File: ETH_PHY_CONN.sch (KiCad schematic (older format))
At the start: 63 parts, among them J2 RJMG2012211A0FR, U7 DP83869HMRGZT, Y1 XRCGE25M000FBA1AR0

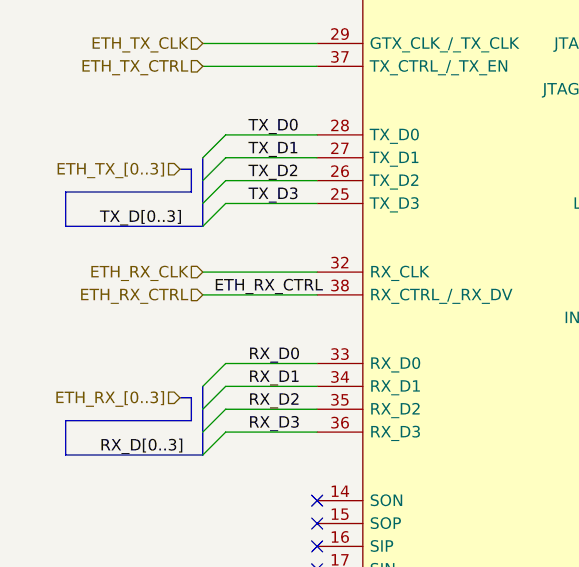
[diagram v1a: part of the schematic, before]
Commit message: Connected USB2 connections with FPGA and updated the top sheet
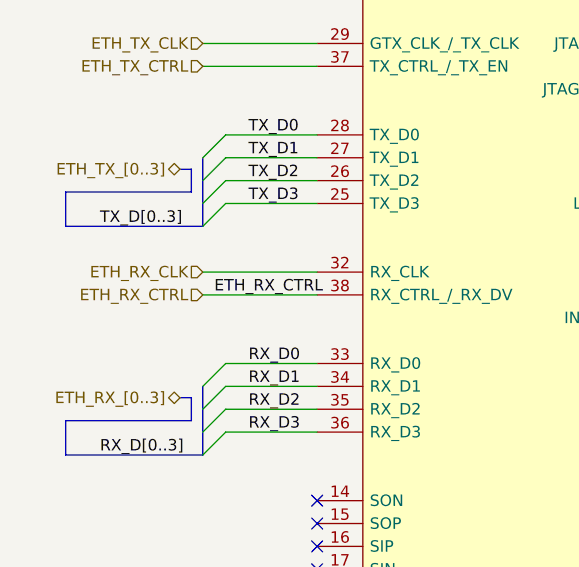
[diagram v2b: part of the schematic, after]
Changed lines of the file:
@@
 $Descr A4 11693 8268
 encoding utf-8
-Sheet 10 22
+Sheet 9 22
 Title ""
 Date ""
@@
 Entry Wire Line
 	1200 5400 1300 5300
-Text HLabel 1100 5450 0    50   Input ~ 0
+Text HLabel 1100 5450 0    50   BiDi ~ 0
 ETH_TX_[0..3]
 Text Label 750  5700 0    50   ~ 0
@@
 Entry Wire Line
 	1200 6400 1300 6300
-Text HLabel 1100 6450 0    50   Input ~ 0
+Text HLabel 1100 6450 0    50   BiDi ~ 0
 ETH_RX_[0..3]
 Text Label 750  6700 0    50   ~ 0

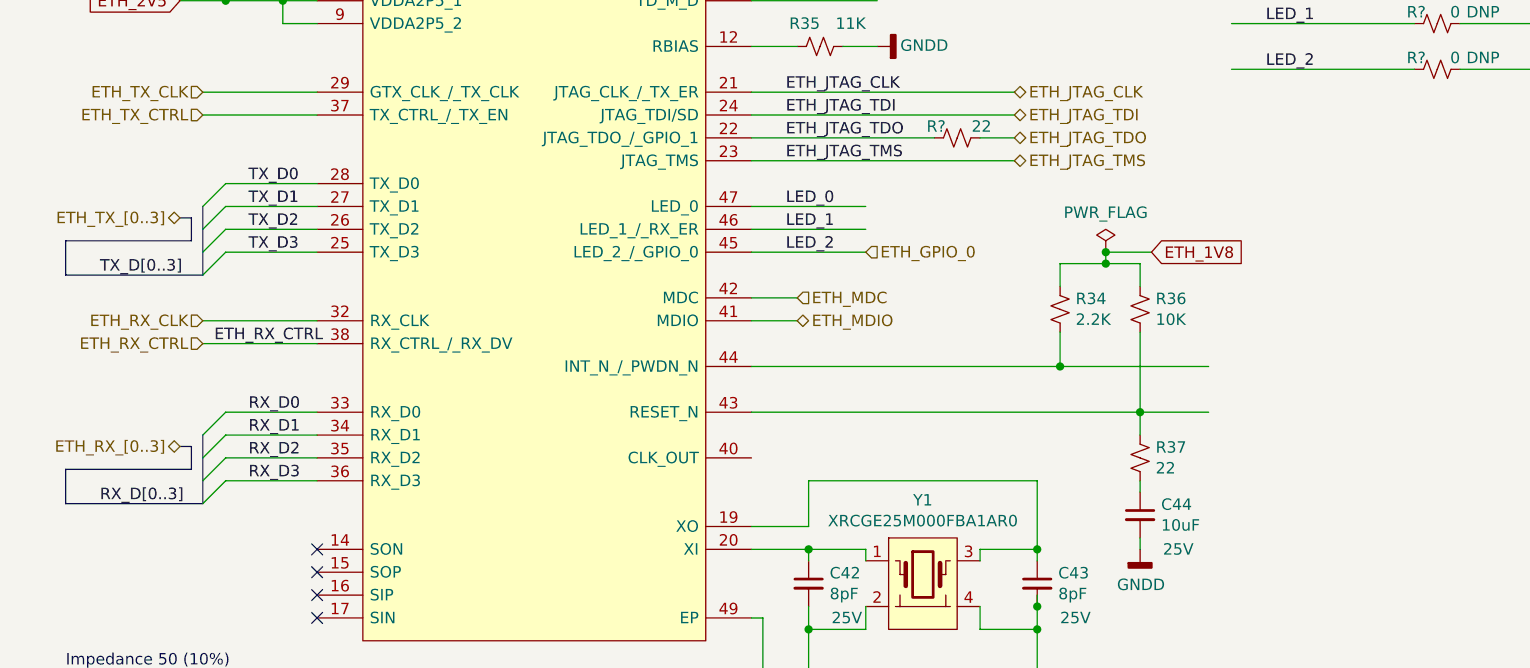
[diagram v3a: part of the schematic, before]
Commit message: Connected Ethernet sheet with FPGA bank
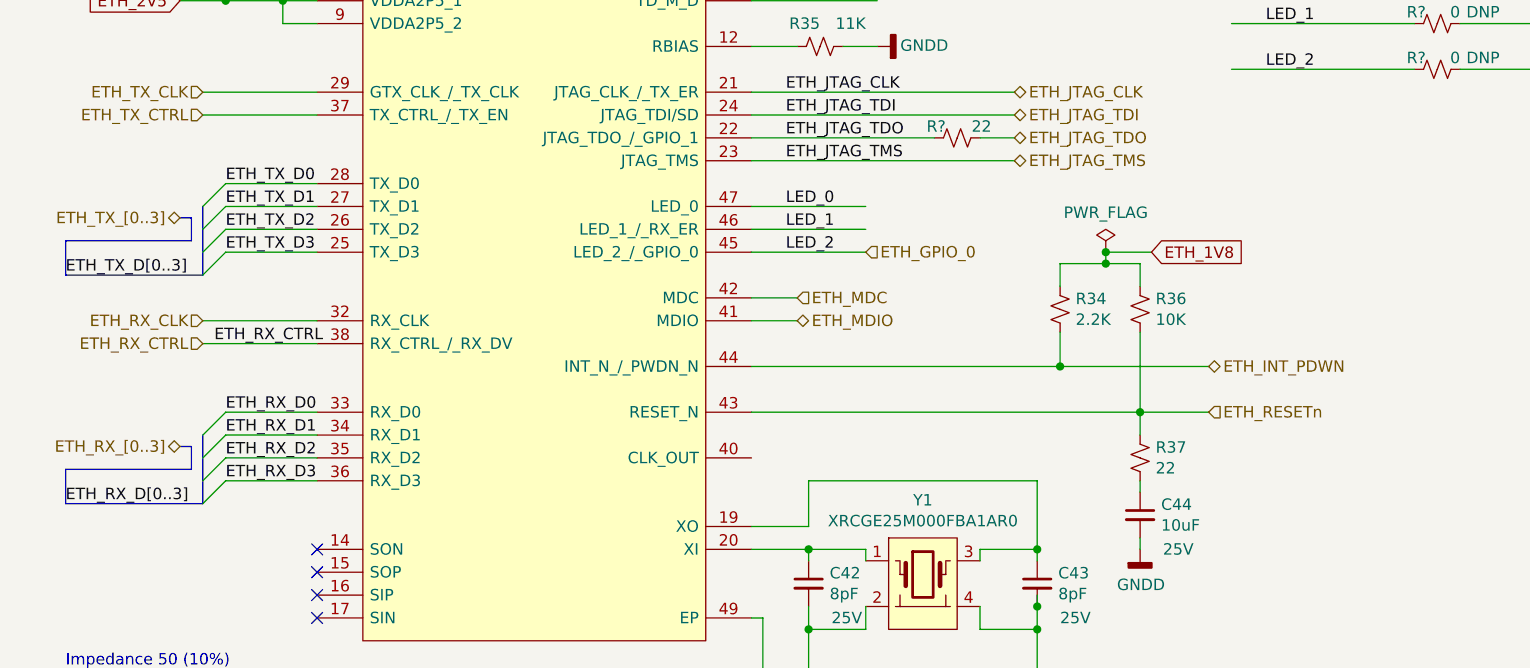
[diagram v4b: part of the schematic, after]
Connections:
- net labels added: ETH_INT_PDWN, ETH_RESETn, ETH_RX_D0, ETH_RX_D1, ETH_RX_D2, ETH_RX_D3, ETH_RX_D[0..3], ETH_TX_D0, ETH_TX_D1, ETH_TX_D2, ETH_TX_D3, ETH_TX_D[0..3]
- net labels removed: RX_D[0..3], TX_D0, TX_D1, TX_D2, TX_D3, TX_D[0..3]

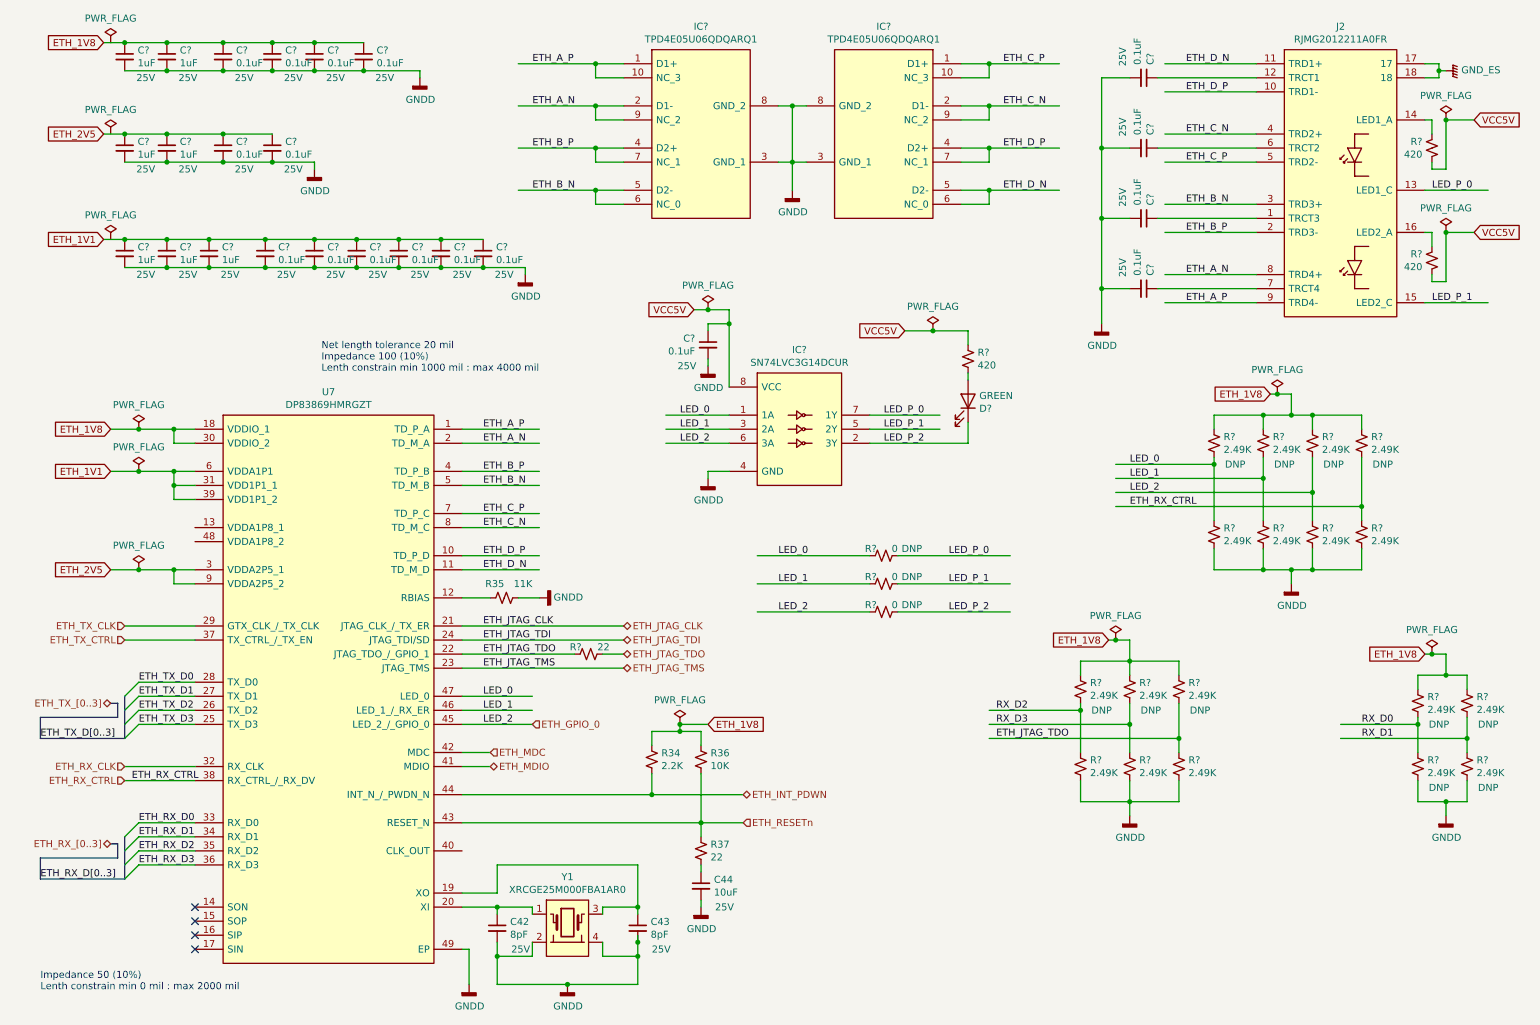
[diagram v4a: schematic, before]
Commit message: PCB created and schematics annotated High speed connections added to the BTB
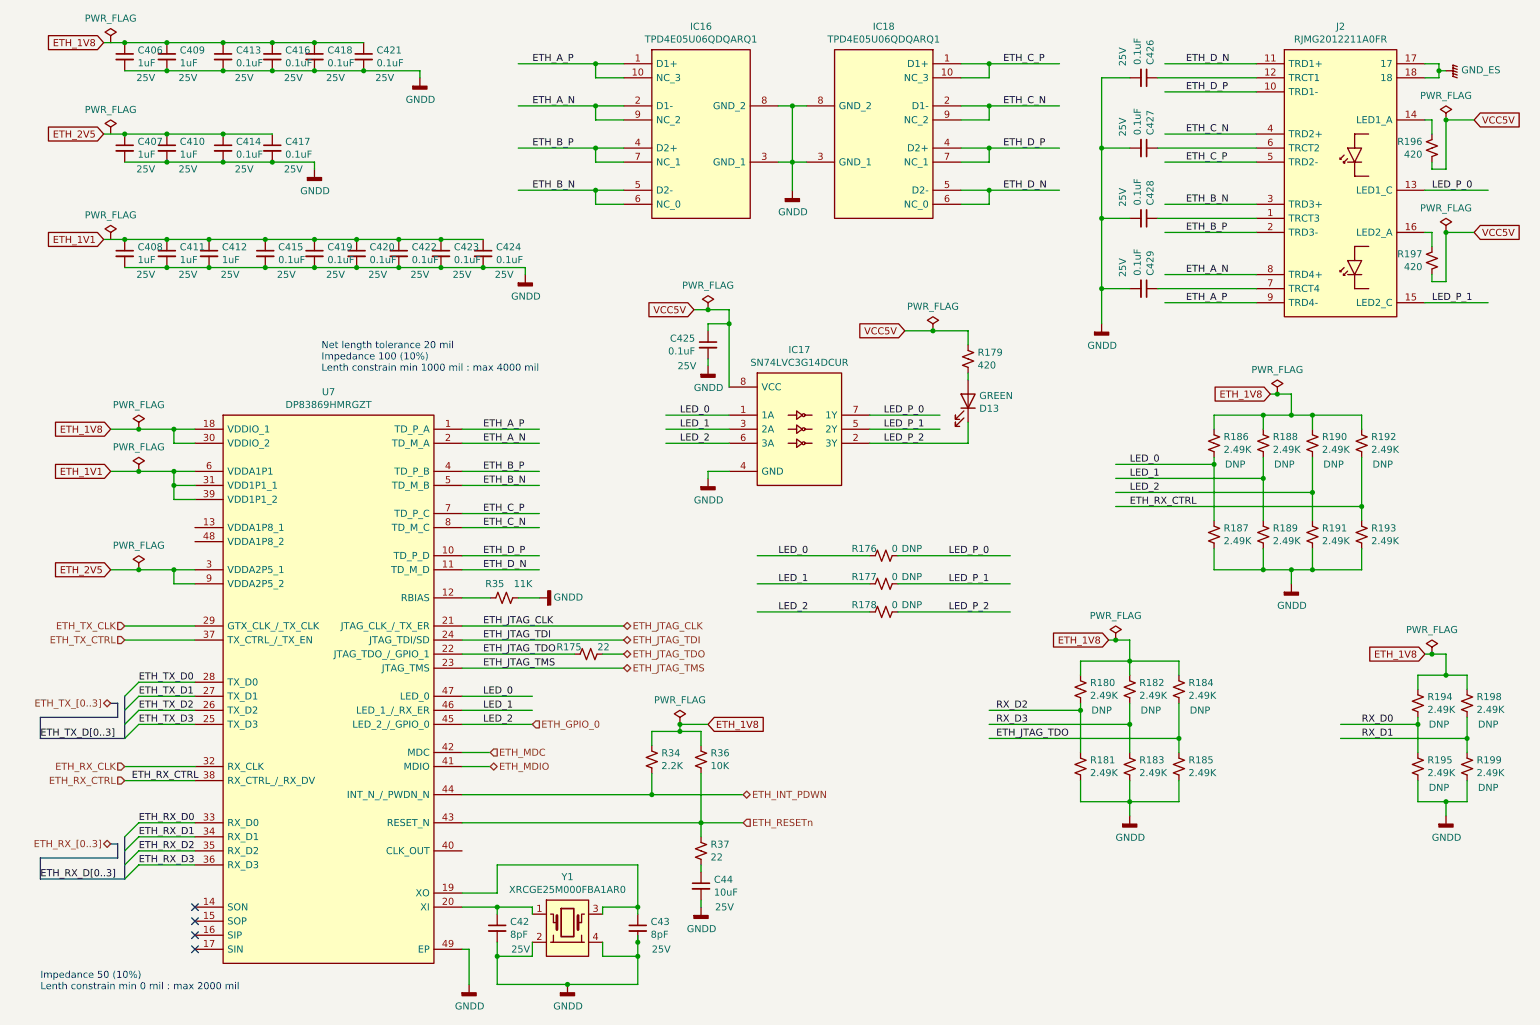
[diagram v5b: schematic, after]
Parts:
- gave numbers to parts that had none: 53

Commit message: Corrected PCB import errors
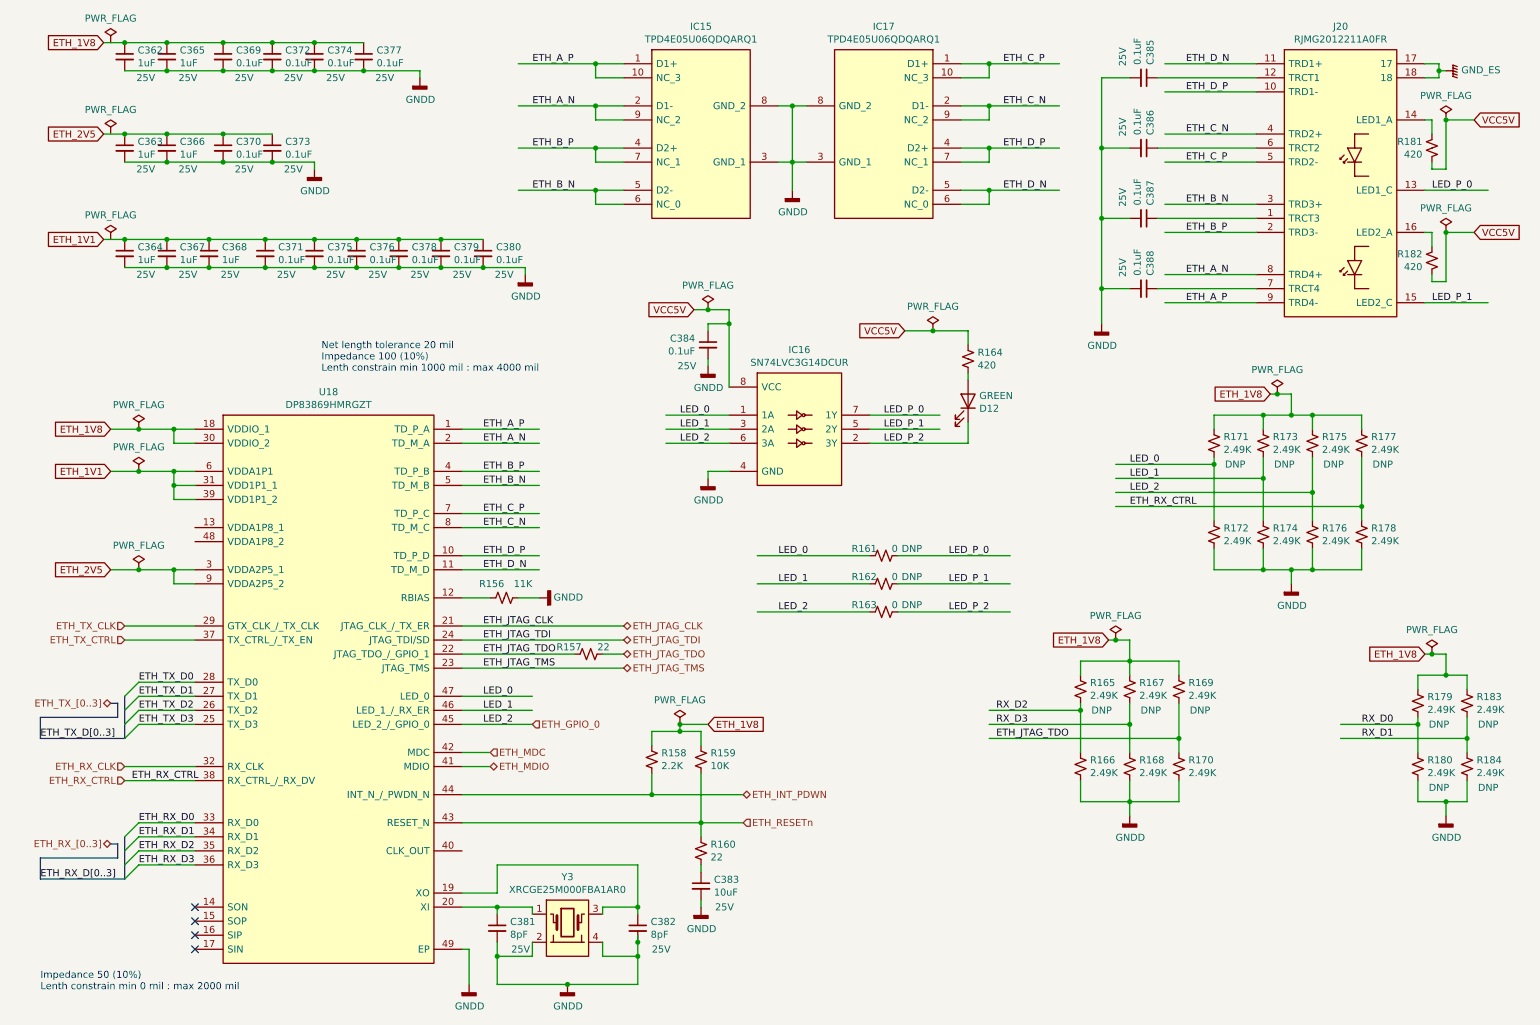
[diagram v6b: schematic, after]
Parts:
- J20: renamed from J2; footprint Connector_RJ:RJ45_Amphenol_RJMG2012211A0FR -> GM_Connectors:RJMG2012211A0FR
- renumbered C406 to C362, C407 to C363, C408 to C364, C409 to C365, C410 to C366, C411 to C367, C412 to C368, C413 to C369, C414 to C370, C415 to C371, C416 to C372, C417 to C373, C418 to C374, C419 to C375, C420 to C376, C421 to C377, C422 to C378, C423 to C379, C424 to C380, C42 to C381, C43 to C382, C44 to C383, C425 to C384, C426 to C385, C427 to C386, C428 to C387, C429 to C388, D13 to D12, IC16 to IC15, IC17 to IC16, IC18 to IC17, R35 to R156, R175 to R157, R34 to R158, R36 to R159, R37 to R160, R176 to R161, R177 to R162, R178 to R163, R179 to R164, R180 to R165, R181 to R166, R182 to R167, R183 to R168, R184 to R169, R185 to R170, R186 to R171, R187 to R172, R188 to R173, R189 to R174, R190 to R175, R191 to R176, R192 to R177, R193 to R178, R194 to R179, R195 to R180, R196 to R181, R197 to R182, R198 to R183, R199 to R184, U7 to U18, Y1 to Y3
